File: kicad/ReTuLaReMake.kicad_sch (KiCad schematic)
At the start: 23 parts, among them J1 40 Pin DIP Header, U1 ATF1508AS-10AU100

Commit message: KiCAD: Move PA0
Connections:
- net PA0: now also U1.41 (I/O/PD2); no longer U1.49 (I/O_37)
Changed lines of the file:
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@@
   (no_connect (at 66.04 99.06))
   (no_connect (at 142.24 96.52))
-  (no_connect (at 111.76 149.86))
+  (no_connect (at 132.08 149.86))
   (wire (pts (xy 255.27 97.79) (xy 233.68 97.79))
     (stroke (width 0) (type default) (color 0 0 0 0))
@@
     (effects (font (size 1.27 1.27)) (justify right bottom))
   )
-  (label "PA0" (at 132.08 149.86 270)
-    (effects (font (size 1.27 1.27)) (justify right bottom))
-  )
+  (label "PA0" (at 111.76 149.86 270)
+    (effects (font (size 1.27 1.27)) (justify right bottom))
+  )

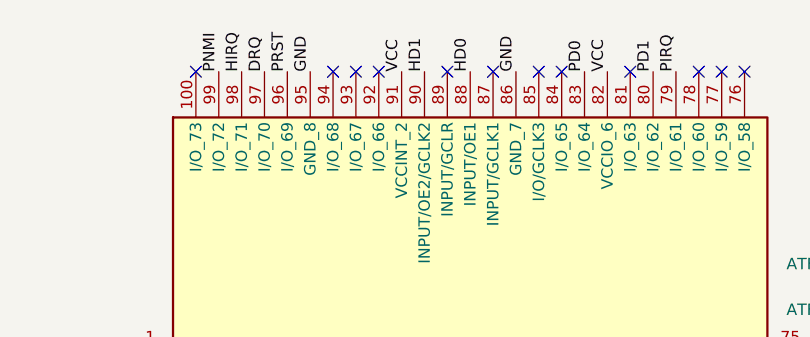
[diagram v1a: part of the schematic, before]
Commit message: KiCAD: Move HD1/0 to valid pins
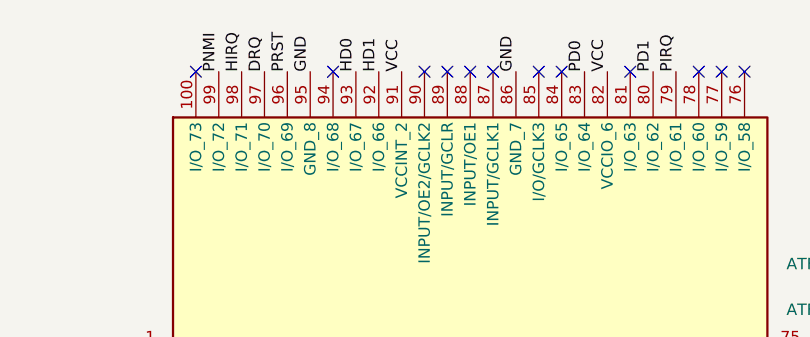
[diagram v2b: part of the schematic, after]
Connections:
- net HD0: now also U1.93 (I/O_67); no longer U1.88 (INPUT/OE1)
- net HD1: now also U1.92 (I/O_66); no longer U1.90 (INPUT/OE2/GCLK2)
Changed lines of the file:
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@@
   (no_connect (at 66.04 119.38))
   (no_connect (at 66.04 121.92))
-  (no_connect (at 93.98 38.1))
+  (no_connect (at 104.14 38.1))
   (no_connect (at 109.22 149.86))
   (no_connect (at 66.04 109.22))
@@
   (no_connect (at 142.24 86.36))
   (no_connect (at 167.64 66.04))
-  (no_connect (at 91.44 38.1))
+  (no_connect (at 99.06 38.1))
   (no_connect (at 66.04 78.74))
   (no_connect (at 142.24 114.3))
@@
     (effects (font (size 1.27 1.27)) (justify right bottom))
   )
-  (label "HD0" (at 104.14 38.1 90)
+  (label "HD0" (at 91.44 38.1 90)
     (effects (font (size 1.27 1.27)) (justify left bottom))
   )
@@
     (effects (font (size 1.27 1.27)) (justify right bottom))
   )
-  (label "HD1" (at 99.06 38.1 90)
-    (effects (font (size 1.27 1.27)) (justify left bottom))
-  )
+  (label "HD1" (at 93.98 38.1 90)
+    (effects (font (size 1.27 1.27)) (justify left bottom))
+  )

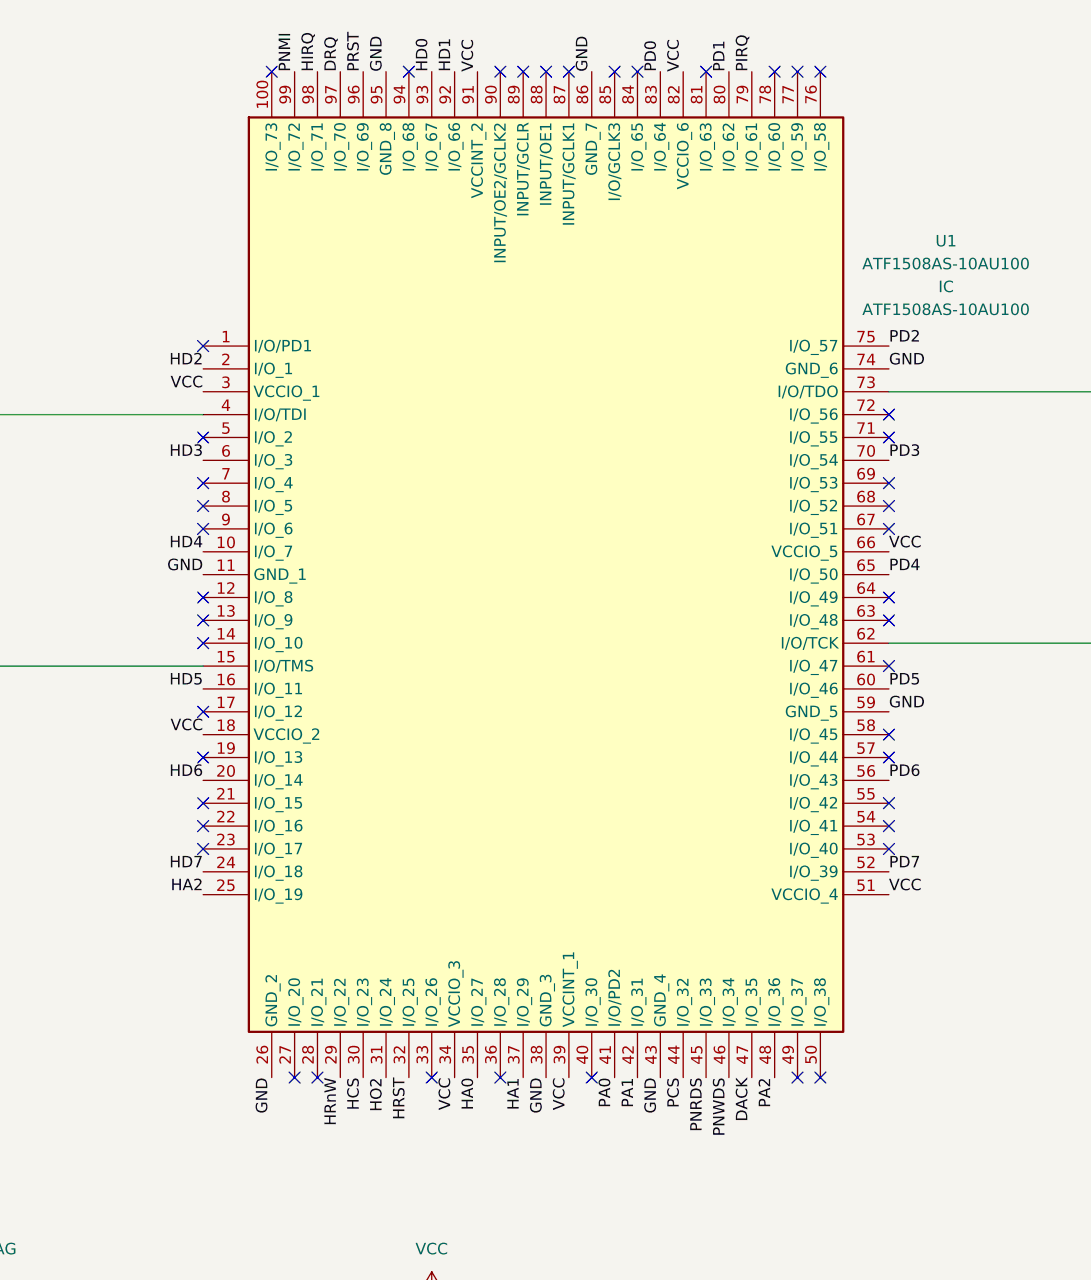
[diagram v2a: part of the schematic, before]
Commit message: KiCAD: Correct pin assignments to match JK's PCBs
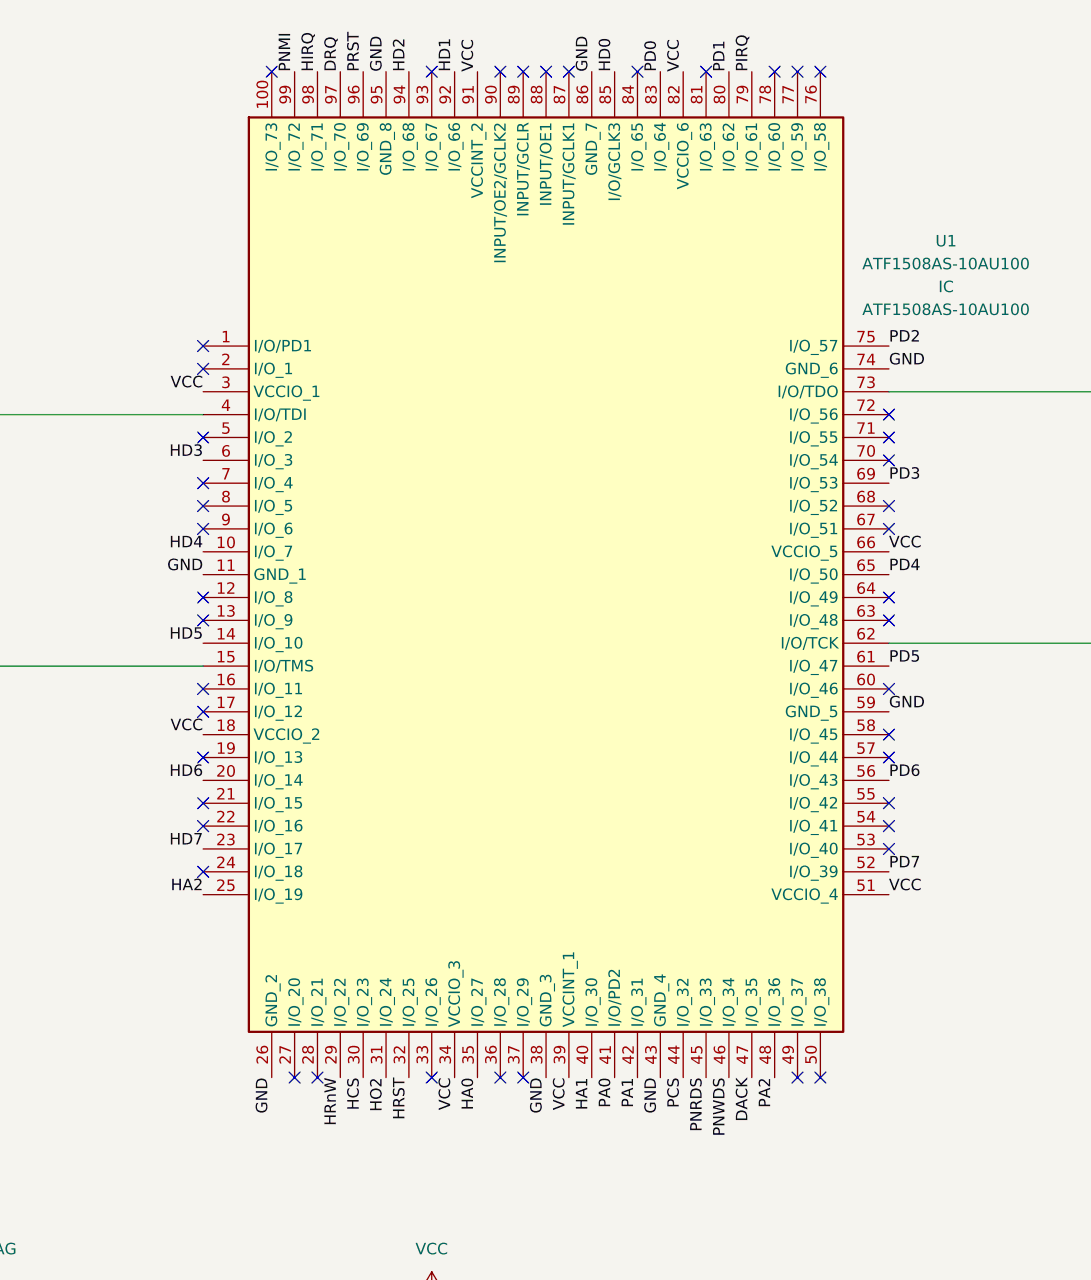
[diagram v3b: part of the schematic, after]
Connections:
- net HA1: now also U1.40 (I/O_30); no longer U1.37 (I/O_29)
- net HD0: now also U1.85 (I/O/GCLK3); no longer U1.93 (I/O_67)
- net HD2: now also U1.94 (I/O_68); no longer U1.2 (I/O_1)
- net HD5: now also U1.14 (I/O_10); no longer U1.16 (I/O_11)
- net HD7: now also U1.23 (I/O_17); no longer U1.24 (I/O_18)
- net PD3: now also U1.69 (I/O_53); no longer U1.70 (I/O_54)
- net PD5: now also U1.61 (I/O_47); no longer U1.60 (I/O_46)
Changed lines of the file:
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@@
   (no_connect (at 142.24 78.74))
   (no_connect (at 142.24 121.92))
-  (no_connect (at 66.04 101.6))
+  (no_connect (at 66.04 106.68))
   (no_connect (at 73.66 38.1))
   (no_connect (at 255.27 80.01))
@@
   (no_connect (at 255.27 77.47))
   (no_connect (at 66.04 83.82))
-  (no_connect (at 142.24 83.82))
+  (no_connect (at 142.24 81.28))
   (no_connect (at 142.24 111.76))
   (no_connect (at 132.08 38.1))
   (no_connect (at 66.04 86.36))
+  (no_connect (at 66.04 68.58))
   (no_connect (at 134.62 149.86))
   (no_connect (at 66.04 88.9))
+  (no_connect (at 66.04 71.12))
   (no_connect (at 99.06 149.86))
-  (no_connect (at 66.04 68.58))
   (no_connect (at 142.24 99.06))
   (no_connect (at 78.74 149.86))
@@
   (no_connect (at 66.04 121.92))
   (no_connect (at 104.14 38.1))
-  (no_connect (at 109.22 149.86))
+  (no_connect (at 101.6 149.86))
   (no_connect (at 66.04 109.22))
   (no_connect (at 106.68 38.1))
   (no_connect (at 134.62 38.1))
-  (no_connect (at 142.24 104.14))
+  (no_connect (at 142.24 106.68))
   (no_connect (at 66.04 114.3))
   (no_connect (at 121.92 38.1))
-  (no_connect (at 88.9 38.1))
+  (no_connect (at 91.44 38.1))
   (no_connect (at 142.24 124.46))
   (no_connect (at 142.24 86.36))
@@
   (no_connect (at 66.04 78.74))
   (no_connect (at 142.24 114.3))
-  (no_connect (at 66.04 124.46))
+  (no_connect (at 66.04 127))
   (no_connect (at 91.44 149.86))
-  (no_connect (at 111.76 38.1))
   (no_connect (at 66.04 99.06))
   (no_connect (at 142.24 96.52))
@@
     (effects (font (size 1.27 1.27)) (justify right bottom))
   )
-  (label "HD5" (at 66.04 106.68 180)
+  (label "HD5" (at 66.04 101.6 180)
     (effects (font (size 1.27 1.27)) (justify right bottom))
   )
@@
     (effects (font (size 1.27 1.27)) (justify left bottom))
   )
-  (label "HD7" (at 66.04 127 180)
+  (label "HD7" (at 66.04 124.46 180)
     (effects (font (size 1.27 1.27)) (justify right bottom))
   )
@@
     (effects (font (size 1.27 1.27)) (justify left bottom))
   )
-  (label "PD5" (at 142.24 106.68 0)
+  (label "PD5" (at 142.24 104.14 0)
     (effects (font (size 1.27 1.27)) (justify left bottom))
   )
@@
     (effects (font (size 1.27 1.27)) (justify right bottom))
   )
-  (label "HD0" (at 91.44 38.1 90)
+  (label "HD0" (at 111.76 38.1 90)
     (effects (font (size 1.27 1.27)) (justify left bottom))
   )
@@
     (effects (font (size 1.27 1.27)) (justify left bottom))
   )
-  (label "HD2" (at 66.04 71.12 180)
-    (effects (font (size 1.27 1.27)) (justify right bottom))
+  (label "HD2" (at 88.9 38.1 90)
+    (effects (font (size 1.27 1.27)) (justify left bottom))
   )
   (label "HD4" (at 219.71 96.52 180)
@@
     (effects (font (size 1.27 1.27)) (justify right bottom))
   )
-  (label "HA1" (at 101.6 149.86 270)
+  (label "HA1" (at 109.22 149.86 270)
     (effects (font (size 1.27 1.27)) (justify right bottom))
   )
@@
     (effects (font (size 1.27 1.27)) (justify right bottom))
   )
-  (label "PD3" (at 142.24 81.28 0)
-    (effects (font (size 1.27 1.27)) (justify left bottom))
-  )
+  (label "PD3" (at 142.24 83.82 0)
+    (effects (font (size 1.27 1.27)) (justify left bottom))
+  )

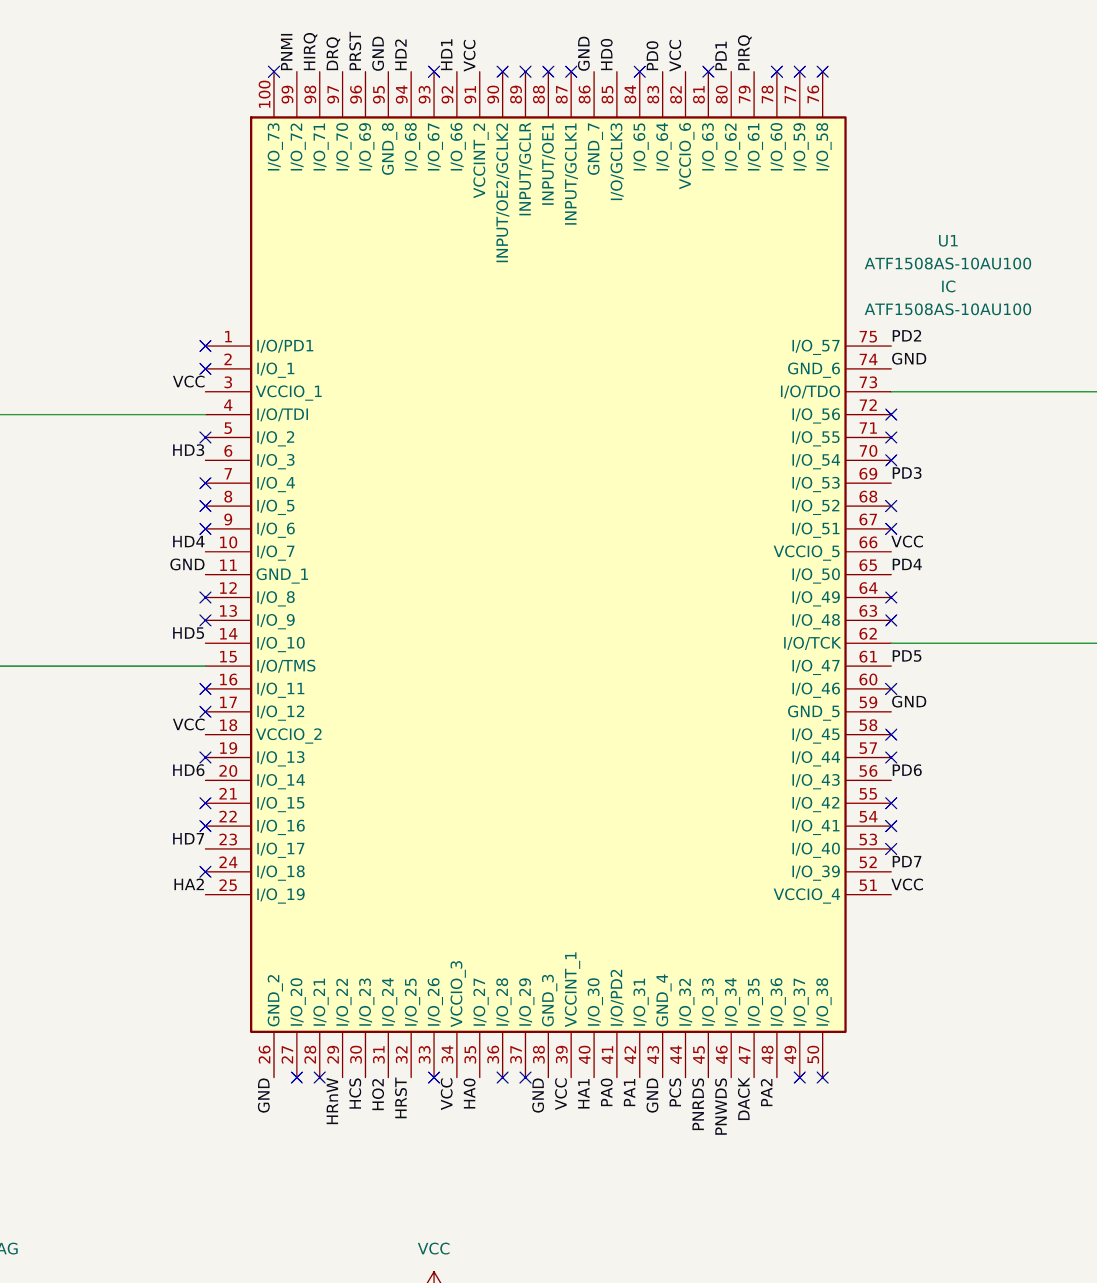
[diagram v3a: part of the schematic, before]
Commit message: KiCAD: Connect unused CPLD pins to GND
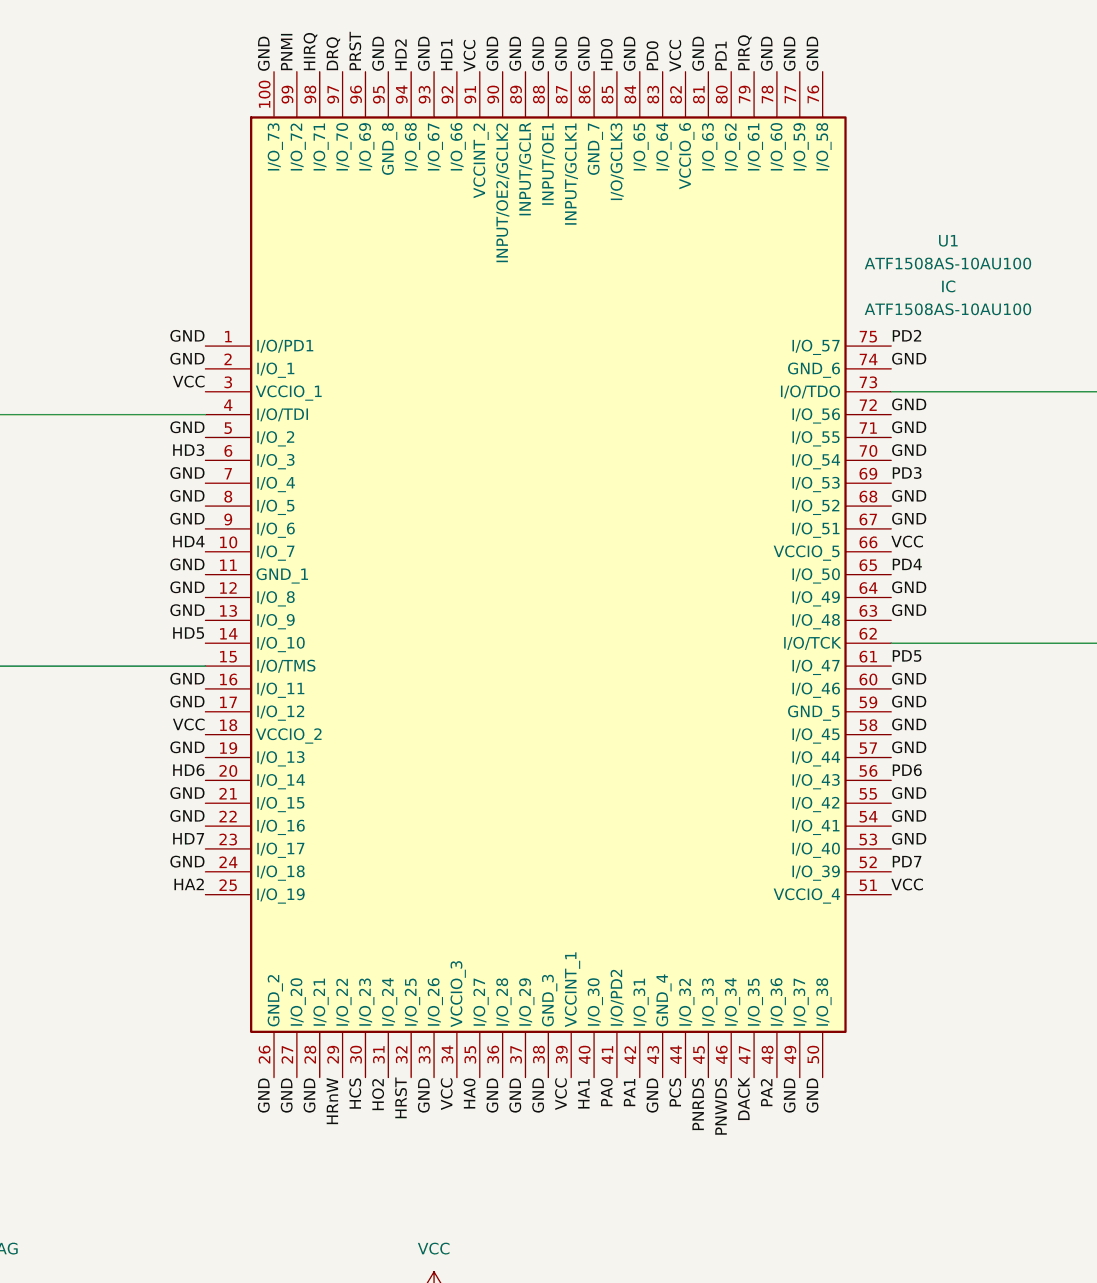
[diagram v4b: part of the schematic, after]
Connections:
- net GND: now also U1.1 (I/O/PD1), U1.100 (I/O_73), U1.12 (I/O_8), U1.13 (I/O_9), U1.16 (I/O_11), U1.17 (I/O_12), U1.19 (I/O_13), U1.2 (I/O_1), U1.21 (I/O_15), U1.22 (I/O_16), U1.24 (I/O_18), U1.27 (I/O_20), U1.28 (I/O_21), U1.33 (I/O_26), U1.36 (I/O_28), U1.37 (I/O_29), U1.49 (I/O_37), U1.5 (I/O_2), U1.50 (I/O_38), U1.53 (I/O_40), U1.54 (I/O_41), U1.55 (I/O_42), U1.57 (I/O_44), U1.58 (I/O_45), U1.60 (I/O_46), U1.63 (I/O_48), U1.64 (I/O_49), U1.67 (I/O_51), U1.68 (I/O_52), U1.7 (I/O_4), U1.70 (I/O_54), U1.71 (I/O_55), U1.72 (I/O_56), U1.76 (I/O_58), U1.77 (I/O_59), U1.78 (I/O_60), U1.8 (I/O_5), U1.81 (I/O_63), U1.84 (I/O_65), U1.87 (INPUT/GCLK1), U1.88 (INPUT/OE1), U1.89 (INPUT/GCLR), U1.9 (I/O_6), U1.90 (INPUT/OE2/GCLK2), U1.93 (I/O_67)
- no-connect marks 48 -> 3
